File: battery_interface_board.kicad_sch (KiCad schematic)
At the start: 0 parts

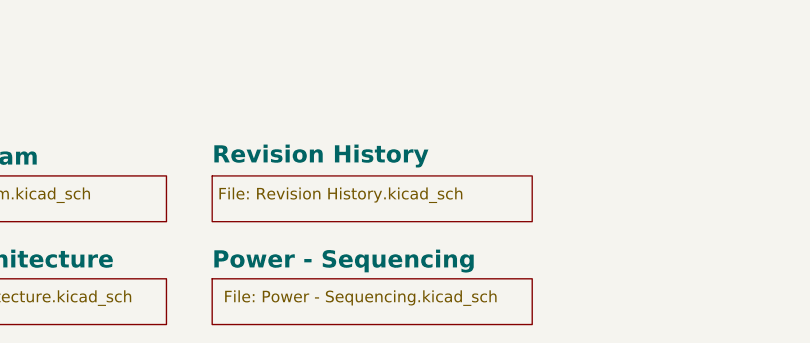
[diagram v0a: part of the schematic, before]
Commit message: PCB[Layout and Routing]: Routing and layout done, changed to micofit connector, need to review and fix drc errors. SCH[Connector & Fuse]: Schmatic for connector, fuse and board to board layout, need to cleanup and add board standoffs.
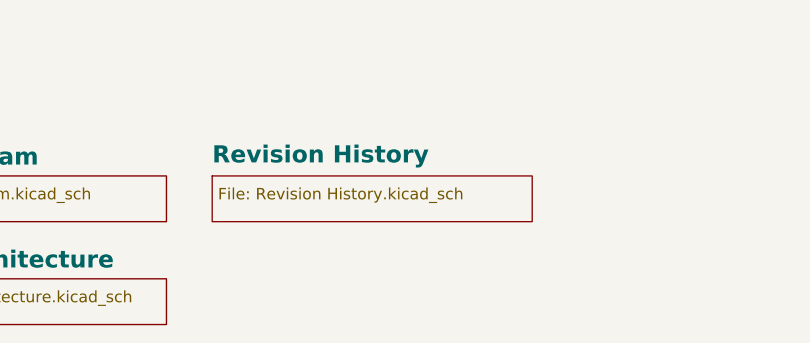
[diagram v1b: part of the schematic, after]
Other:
- removed sheet Power - Sequencing
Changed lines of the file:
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@@
 	(paper "A3")
 	(title_block
-		(date "2025-01-12")
+		(date "2026-10-12")
 		(rev "${REVISION}")
 		(company "${COMPANY}")
@@
 		)
 	)
-	(sheet
-		(at 340.36 313.69)
-		(size 35.56 5.08)
-		(exclude_from_sim no)
-		(in_bom yes)
-		(on_board yes)
-		(dnp no)
-		(stroke
-			(width 0.1524)
-			(type solid)
-		)
-		(fill
-			(color 0 0 0 0)
-		)
-		(property "Sheetname" "Power - Sequencing"
-			(at 340.36 312.6609 0)
-			(show_name no)
-			(do_not_autoplace no)
-			(effects
-				(font
-					(face "Times New Roman")
-					(size 1.905 1.905)
-					(bold yes)
-					(color 0 0 0 1)
-				)
-				(justify left bottom)
-			)
-		)
-		(property "Sheetfile" "Power - Sequencing.kicad_sch"
-			(at 341.63 314.96 0)
-			(show_name no)
-			(do_not_autoplace no)
-			(effects
-				(font
-					(face "Arial")
-					(size 1.27 1.27)
-				)
-				(justify left top)
-			)
-		)
-		(instances
-			(project "battery_interface_board"
-				(path "/f9e05184-c88b-4a88-ae9c-ab2bdb32be7c"
-					(page "6")
-				)
-			)
-		)
-	)

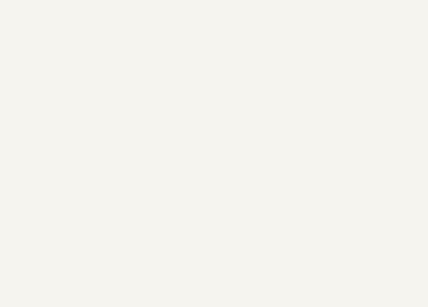
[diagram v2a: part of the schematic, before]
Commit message: PCB[Routing, Mechanical, Silk]: Inital routing, Finalized mounting points and board to board connector reltive posision, and inital silkscreen. SCH[Labels]: Updated labels to match BMS_Slave board.
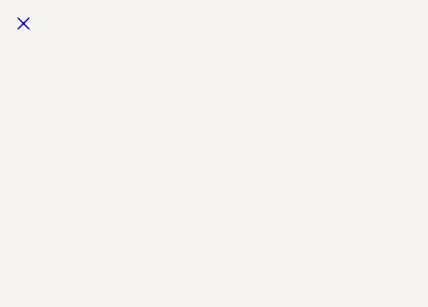
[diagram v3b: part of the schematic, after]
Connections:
- no-connect marks 0 -> 1
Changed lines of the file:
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@@
 		)
+	)
+	(no_connect
+		(at 10.16 -71.12)
 	)
 	(polyline
